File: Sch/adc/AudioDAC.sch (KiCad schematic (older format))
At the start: 22 parts, among them CN3 AudioJack, J7 JP2, U6 NAU8822LYG

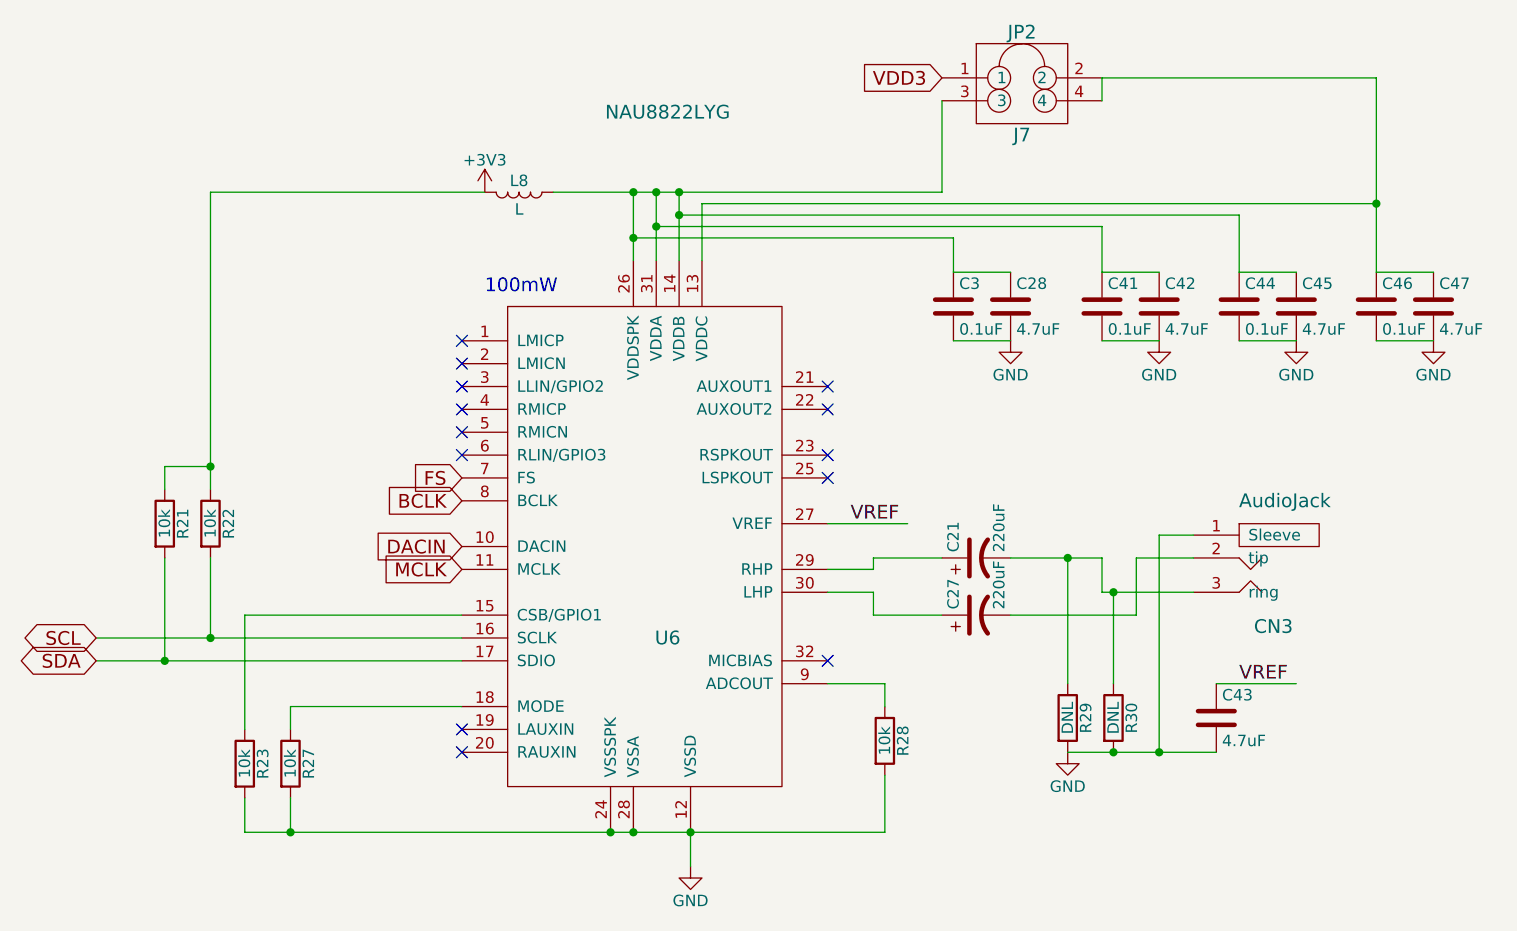
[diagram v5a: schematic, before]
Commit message: Changed TCXO->MEMS TCXO. BOM finished
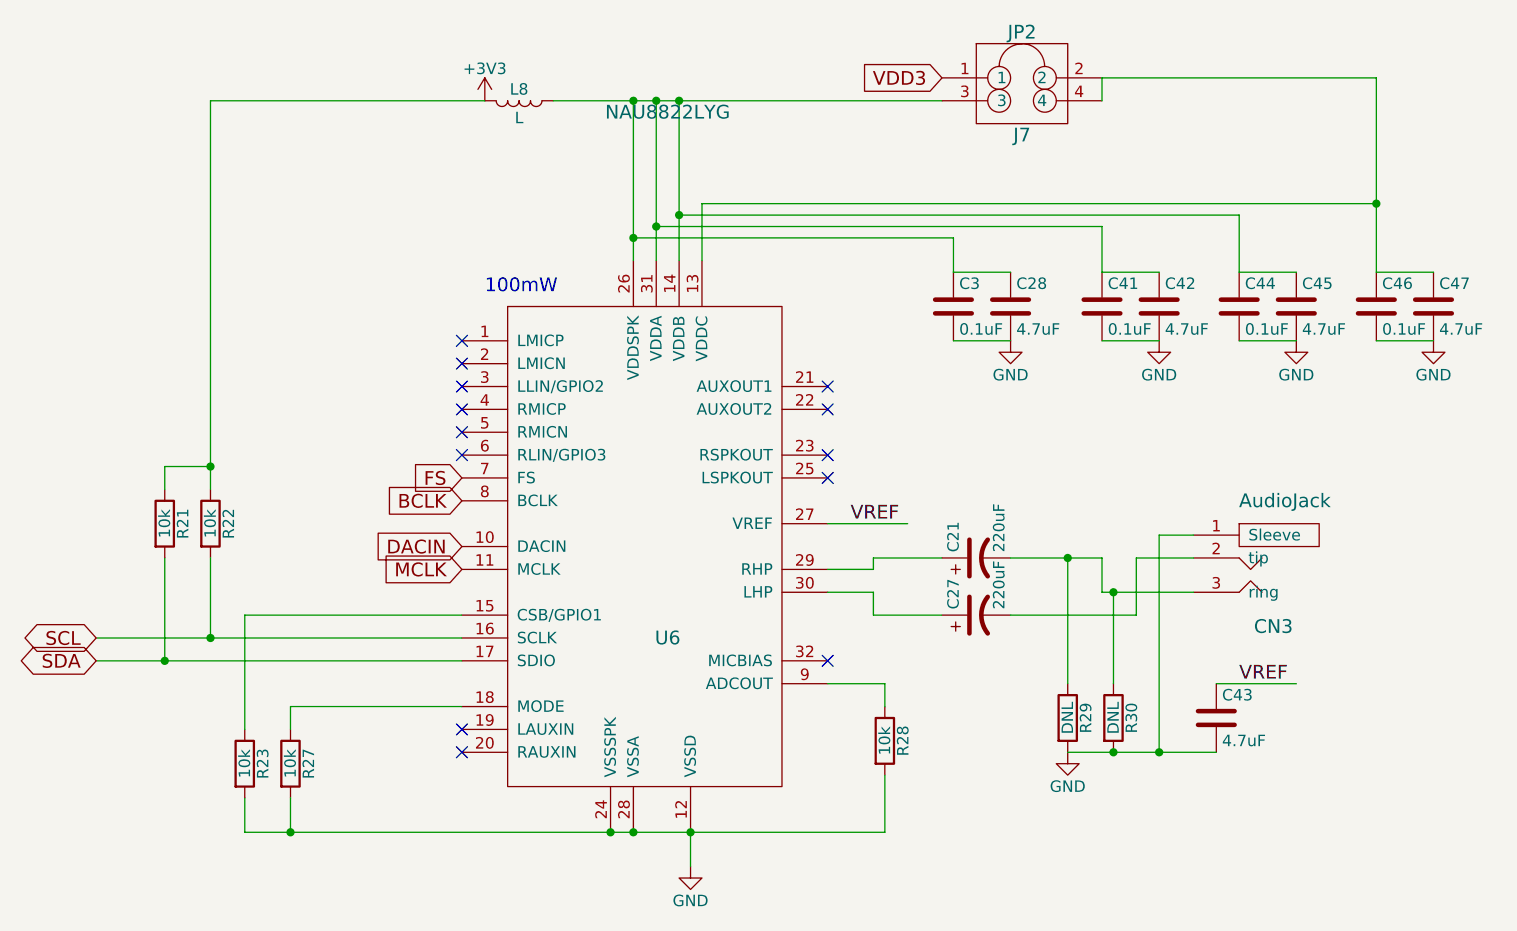
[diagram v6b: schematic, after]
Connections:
- wire segments 62 -> 61
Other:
- moved on the sheet: L8
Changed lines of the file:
@@
 L +3V3 #PWR053
 U 1 1 58A98414
-P 4750 2150
-F 0 "#PWR053" H 4750 2000 50  0001 C CNN
-F 1 "+3V3" H 4750 2290 50  0000 C CNN
-F 2 "" H 4750 2150 50  0000 C CNN
-F 3 "" H 4750 2150 50  0000 C CNN
-	1    4750 2150
+P 4750 1750
+F 0 "#PWR053" H 4750 1600 50  0001 C CNN
+F 1 "+3V3" H 4750 1890 50  0000 C CNN
+F 2 "" H 4750 1750 50  0000 C CNN
+F 3 "" H 4750 1750 50  0000 C CNN
+	1    4750 1750
 	1    0    0    -1
 $EndComp
@@
 L L L8
 U 1 1 58A98450
-P 4900 2150
-F 0 "L8" V 4850 2150 50  0000 C CNN
-F 1 "L" V 4975 2150 50  0000 C CNN
-F 2 "" H 4900 2150 50  0001 C CNN
-F 3 "" H 4900 2150 50  0000 C CNN
-	1    4900 2150
+P 4900 1750
+F 0 "L8" V 4850 1750 50  0000 C CNN
+F 1 "L" V 4975 1750 50  0000 C CNN
+F 2 "" H 4900 1750 50  0001 C CNN
+F 3 "" H 4900 1750 50  0000 C CNN
+	1    4900 1750
 	0    1    1    0
 $EndComp
@@
 Connection ~ 5300 4950
 Wire Wire Line
-	5050 2150 6750 2150
-Wire Wire Line
-	5400 2150 5400 2450
-Wire Wire Line
-	5500 2150 5500 2450
-Connection ~ 5400 2150
-Wire Wire Line
-	5600 2150 5600 2450
-Connection ~ 5500 2150
+	5050 1750 6750 1750
+Wire Wire Line
+	5500 1750 5500 2450
+Wire Wire Line
+	5600 1750 5600 2450
 Wire Wire Line
 	6800 2800 7050 2800
@@
 Wire Wire Line
 	8650 2500 8900 2500
-Connection ~ 5600 2150
 Wire Wire Line
 	8650 1650 8650 2500
@@
 Wire Wire Line
 	8050 2250 8050 2500
-Connection ~ 5600 2250
 Wire Wire Line
 	5500 2300 7450 2300
 Wire Wire Line
 	7450 2300 7450 2500
-Connection ~ 5500 2300
 Wire Wire Line
 	5400 2350 6800 2350
 Wire Wire Line
 	6800 2350 6800 2500
-Connection ~ 5400 2350
 Wire Wire Line
 	4650 4000 3700 4000
@@
 Connection ~ 5650 4950
 Wire Wire Line
-	4650 4100 3050 4100
+	3050 4100 4650 4100
 Wire Wire Line
 	3050 4200 4650 4200
@@
 $EndComp
 Wire Wire Line
-	4750 2150 3550 2150
-Wire Wire Line
-	3550 2150 3550 3450
+	4750 1750 3550 1750
+Wire Wire Line
+	3550 1750 3550 3450
 Wire Wire Line
 	3550 3750 3550 4100
@@
 $EndComp
 Wire Wire Line
-	6750 2150 6750 1750
-Wire Wire Line
 	7450 1750 7450 1650
 Wire Wire Line
@@
 Text Notes 4750 2600 0    60   ~ 0
 100mW
+Wire Wire Line
+	5400 1750 5400 2450
+Connection ~ 5600 1750
+Connection ~ 5600 2250
+Connection ~ 5500 1750
+Connection ~ 5500 2300
+Connection ~ 5400 1750
+Connection ~ 5400 2350
 $EndSCHEMATC

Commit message: Assigned footprint to all the parts
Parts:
- C21, C27: footprint Capacitors_SMD:C_1206 -> adc_lib:C1206
- C28, C42, C43, C45, C47: footprint Capacitors_SMD:C_0603 -> adc_lib:C0603
- C3, C41, C44, C46: footprint Capacitors_SMD:C_0402 -> adc_lib:C0402
- CN3: footprint (none) -> adc_lib:SJ-3523-SMT
- J7: footprint Pin_Headers:Pin_Header_Straight_2x02_Pitch2.54mm -> adc_lib:M20-9980245
- L8: footprint (none) -> adc_lib:FB0805
- R21, R22, R23, R27, R28, R29, R30: footprint Resistors_SMD:R_0603 -> adc_lib:R0603
- U6: footprint (none) -> adc_lib:NAU8822L
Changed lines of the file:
@@
 F 0 "U6" H 5550 2400 60  0000 C CNN
 F 1 "NAU8822LYG" H 5550 4700 60  0000 C CNN
-F 2 "" H 5550 2400 60  0001 C CNN
+F 2 "adc_lib:NAU8822L" H 5550 2400 60  0001 C CNN
 F 3 "" H 5550 2400 60  0001 C CNN
 	1    5550 3250
@@
 F 0 "CN3" H 8200 3450 60  0000 C CNN
 F 1 "AudioJack" H 8250 4000 60  0000 C CNN
-F 2 "" H 8200 3450 60  0001 C CNN
+F 2 "adc_lib:SJ-3523-SMT" H 8200 3450 60  0001 C CNN
 F 3 "" H 8200 3450 60  0001 C CNN
 	1    8250 3750
@@
 F 0 "C21" H 6925 3850 50  0000 L CNN
 F 1 "220uF" H 6925 3650 50  0000 L CNN
-F 2 "Capacitors_SMD:C_1206" H 6900 3750 50  0001 C CNN
+F 2 "adc_lib:C1206" H 6900 3750 50  0001 C CNN
 F 3 "" H 6900 3750 50  0000 C CNN
 	1    6900 3750
@@
 F 0 "C27" H 6925 4100 50  0000 L CNN
 F 1 "220uF" H 6925 3900 50  0000 L CNN
-F 2 "Capacitors_SMD:C_1206" H 6900 4000 50  0001 C CNN
+F 2 "adc_lib:C1206" H 6900 4000 50  0001 C CNN
 F 3 "" H 6900 4000 50  0000 C CNN
 	1    6900 4000
@@
 F 0 "R29" V 7380 4450 50  0000 C CNN
 F 1 "DNL" V 7300 4450 50  0000 C CNN
-F 2 "Resistors_SMD:R_0603" V 7230 4450 50  0001 C CNN
+F 2 "adc_lib:R0603" V 7230 4450 50  0001 C CNN
 F 3 "" H 7300 4450 50  0000 C CNN
 	1    7300 4450
@@
 F 0 "R30" V 7580 4450 50  0000 C CNN
 F 1 "DNL" V 7500 4450 50  0000 C CNN
-F 2 "Resistors_SMD:R_0603" V 7430 4450 50  0001 C CNN
+F 2 "adc_lib:R0603" V 7430 4450 50  0001 C CNN
 F 3 "" H 7500 4450 50  0000 C CNN
 	1    7500 4450
@@
 F 0 "C43" H 7975 4550 50  0000 L CNN
 F 1 "4.7uF" H 7975 4350 50  0000 L CNN
-F 2 "Capacitors_SMD:C_0603" H 7988 4300 50  0001 C CNN
+F 2 "adc_lib:C0603" H 7988 4300 50  0001 C CNN
 F 3 "" H 7950 4450 50  0000 C CNN
 	1    7950 4450
@@
 F 0 "R27" V 3980 4650 50  0000 C CNN
 F 1 "10k" V 3900 4650 50  0000 C CNN
-F 2 "Resistors_SMD:R_0603" V 3830 4650 50  0001 C CNN
+F 2 "adc_lib:R0603" V 3830 4650 50  0001 C CNN
 F 3 "" H 3900 4650 50  0000 C CNN
 	1    3900 4650
@@
 F 0 "L8" V 4850 1750 50  0000 C CNN
 F 1 "L" V 4975 1750 50  0000 C CNN
-F 2 "" H 4900 1750 50  0001 C CNN
+F 2 "adc_lib:FB0805" H 4900 1750 50  0001 C CNN
 F 3 "" H 4900 1750 50  0000 C CNN
 	1    4900 1750
@@
 F 0 "C28" H 7075 2750 50  0000 L CNN
 F 1 "4.7uF" H 7075 2550 50  0000 L CNN
-F 2 "Capacitors_SMD:C_0603" H 7088 2500 50  0001 C CNN
+F 2 "adc_lib:C0603" H 7088 2500 50  0001 C CNN
 F 3 "" H 7050 2650 50  0000 C CNN
 	1    7050 2650
@@
 F 0 "C3" H 6825 2750 50  0000 L CNN
 F 1 "0.1uF" H 6825 2550 50  0000 L CNN
-F 2 "Capacitors_SMD:C_0402" H 6838 2500 50  0001 C CNN
+F 2 "adc_lib:C0402" H 6838 2500 50  0001 C CNN
 F 3 "" H 6800 2650 50  0000 C CNN
 	1    6800 2650
@@
 F 0 "C42" H 7725 2750 50  0000 L CNN
 F 1 "4.7uF" H 7725 2550 50  0000 L CNN
-F 2 "Capacitors_SMD:C_0603" H 7738 2500 50  0001 C CNN
+F 2 "adc_lib:C0603" H 7738 2500 50  0001 C CNN
 F 3 "" H 7700 2650 50  0000 C CNN
 	1    7700 2650
@@
 F 0 "C41" H 7475 2750 50  0000 L CNN
 F 1 "0.1uF" H 7475 2550 50  0000 L CNN
-F 2 "Capacitors_SMD:C_0402" H 7488 2500 50  0001 C CNN
+F 2 "adc_lib:C0402" H 7488 2500 50  0001 C CNN
 F 3 "" H 7450 2650 50  0000 C CNN
 	1    7450 2650
@@
 F 0 "C45" H 8325 2750 50  0000 L CNN
 F 1 "4.7uF" H 8325 2550 50  0000 L CNN
-F 2 "Capacitors_SMD:C_0603" H 8338 2500 50  0001 C CNN
+F 2 "adc_lib:C0603" H 8338 2500 50  0001 C CNN
 F 3 "" H 8300 2650 50  0000 C CNN
 	1    8300 2650
@@
 F 0 "C44" H 8075 2750 50  0000 L CNN
 F 1 "0.1uF" H 8075 2550 50  0000 L CNN
-F 2 "Capacitors_SMD:C_0402" H 8088 2500 50  0001 C CNN
+F 2 "adc_lib:C0402" H 8088 2500 50  0001 C CNN
 F 3 "" H 8050 2650 50  0000 C CNN
 	1    8050 2650
@@
 F 0 "C47" H 8925 2750 50  0000 L CNN
 F 1 "4.7uF" H 8925 2550 50  0000 L CNN
-F 2 "Capacitors_SMD:C_0603" H 8938 2500 50  0001 C CNN
+F 2 "adc_lib:C0603" H 8938 2500 50  0001 C CNN
 F 3 "" H 8900 2650 50  0000 C CNN
 	1    8900 2650
@@
 F 0 "C46" H 8675 2750 50  0000 L CNN
 F 1 "0.1uF" H 8675 2550 50  0000 L CNN
-F 2 "Capacitors_SMD:C_0402" H 8688 2500 50  0001 C CNN
+F 2 "adc_lib:C0402" H 8688 2500 50  0001 C CNN
 F 3 "" H 8650 2650 50  0000 C CNN
 	1    8650 2650
@@
 F 0 "R23" V 3780 4650 50  0000 C CNN
 F 1 "10k" V 3700 4650 50  0000 C CNN
-F 2 "Resistors_SMD:R_0603" V 3630 4650 50  0001 C CNN
+F 2 "adc_lib:R0603" V 3630 4650 50  0001 C CNN
 F 3 "" H 3700 4650 50  0000 C CNN
 	1    3700 4650
@@
 F 0 "R28" V 6580 4550 50  0000 C CNN
 F 1 "10k" V 6500 4550 50  0000 C CNN
-F 2 "Resistors_SMD:R_0603" V 6430 4550 50  0001 C CNN
+F 2 "adc_lib:R0603" V 6430 4550 50  0001 C CNN
 F 3 "" H 6500 4550 50  0000 C CNN
 	1    6500 4550
@@
 F 0 "R22" V 3630 3600 50  0000 C CNN
 F 1 "10k" V 3550 3600 50  0000 C CNN
-F 2 "Resistors_SMD:R_0603" V 3480 3600 50  0001 C CNN
+F 2 "adc_lib:R0603" V 3480 3600 50  0001 C CNN
 F 3 "" H 3550 3600 50  0000 C CNN
 	1    3550 3600
@@
 F 0 "R21" V 3430 3600 50  0000 C CNN
 F 1 "10k" V 3350 3600 50  0000 C CNN
-F 2 "Resistors_SMD:R_0603" V 3280 3600 50  0001 C CNN
+F 2 "adc_lib:R0603" V 3280 3600 50  0001 C CNN
 F 3 "" H 3350 3600 50  0000 C CNN
 	1    3350 3600
@@
 F 0 "J7" H 7100 1400 60  0000 C CNN
 F 1 "JP2" H 7100 1850 60  0000 C CNN
-F 2 "Pin_Headers:Pin_Header_Straight_2x02_Pitch2.54mm" H 7050 1750 60  0001 C CNN
+F 2 "adc_lib:M20-9980245" H 7050 1750 60  0001 C CNN
 F 3 "" H 7050 1750 60  0001 C CNN
 	1    7100 1650

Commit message: Routing in progress
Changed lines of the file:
@@
 	7600 3750 7850 3750
-Wire Wire Line
-	7050 3750 7450 3750
 Wire Wire Line
 	7450 3750 7450 3900
 Wire Wire Line
 	7450 3900 7850 3900
-Wire Wire Line
-	7300 4300 7300 3750
-Connection ~ 7300 3750
 Wire Wire Line
 	7500 4300 7500 3900
@@
 Connection ~ 5400 1750
 Connection ~ 5400 2350
+Wire Wire Line
+	7300 4300 7300 4000
+Wire Wire Line
+	7050 3750 7450 3750
+Connection ~ 7300 4000
 $EndSCHEMATC
